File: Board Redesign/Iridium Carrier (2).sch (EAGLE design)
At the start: 154 parts, among them J1 Molex 0541020404, J2 SIM Holder, J3 455-1750-1-ND, J4 CORTEX_DEBUG_SMD, J5 USB_MINI-B_SMT, J6 GND, J7 JST-PA-06-RT, J8 U.FL, Q1 2N7002, Q2 2N7002, Q3 2N7002, U1 LT3959, U2 DAVID-HANDY_ON_NCN4555DEFAULT, U3 TXB0108PWR, U4 ATSAMD21G-A, U5 TXB0108PWR, U6 SX1509, U7 TXB0104RUTR, U8 MCP1826T-3302E/DC, X1 43650-0200, X3 C-GRID-09-70543, Y1 32.768kHz

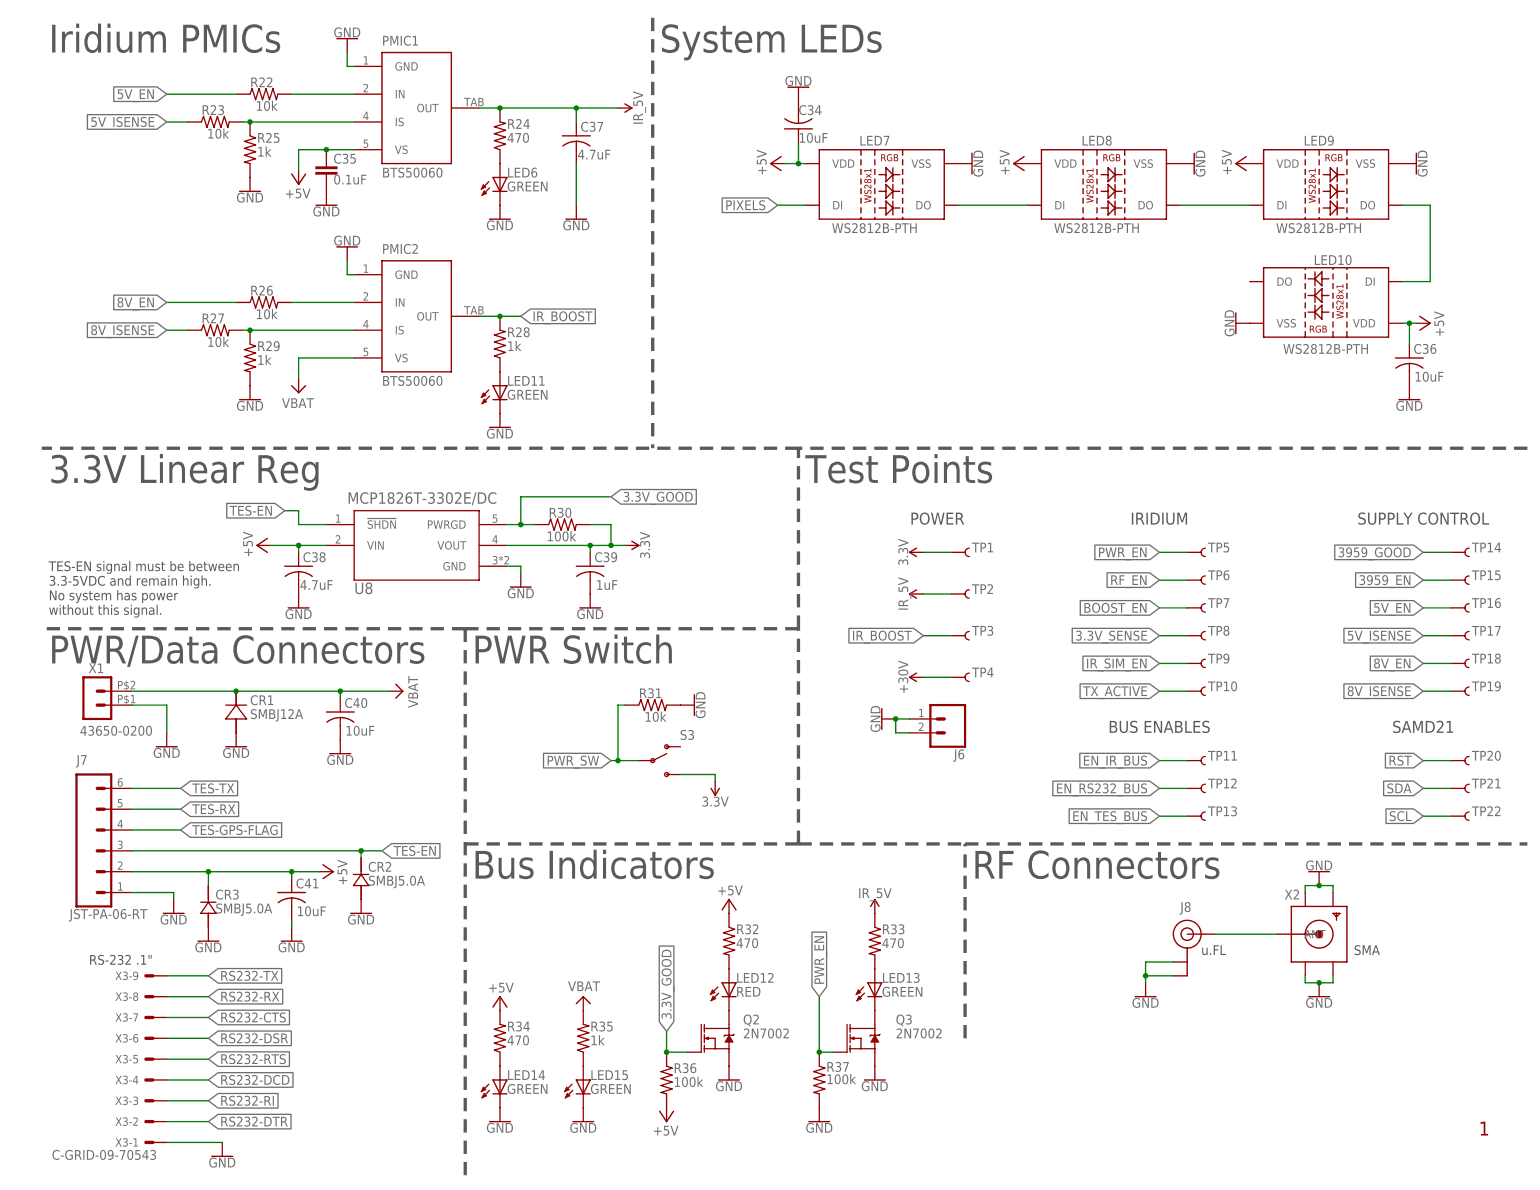
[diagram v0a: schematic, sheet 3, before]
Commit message: Made more progress on board redesign
- Primarily deleted useless (for our purposes) items from the old schematic so we do not have to spend time transferring them over.
- Finished some component transfer
- Renamed some folders
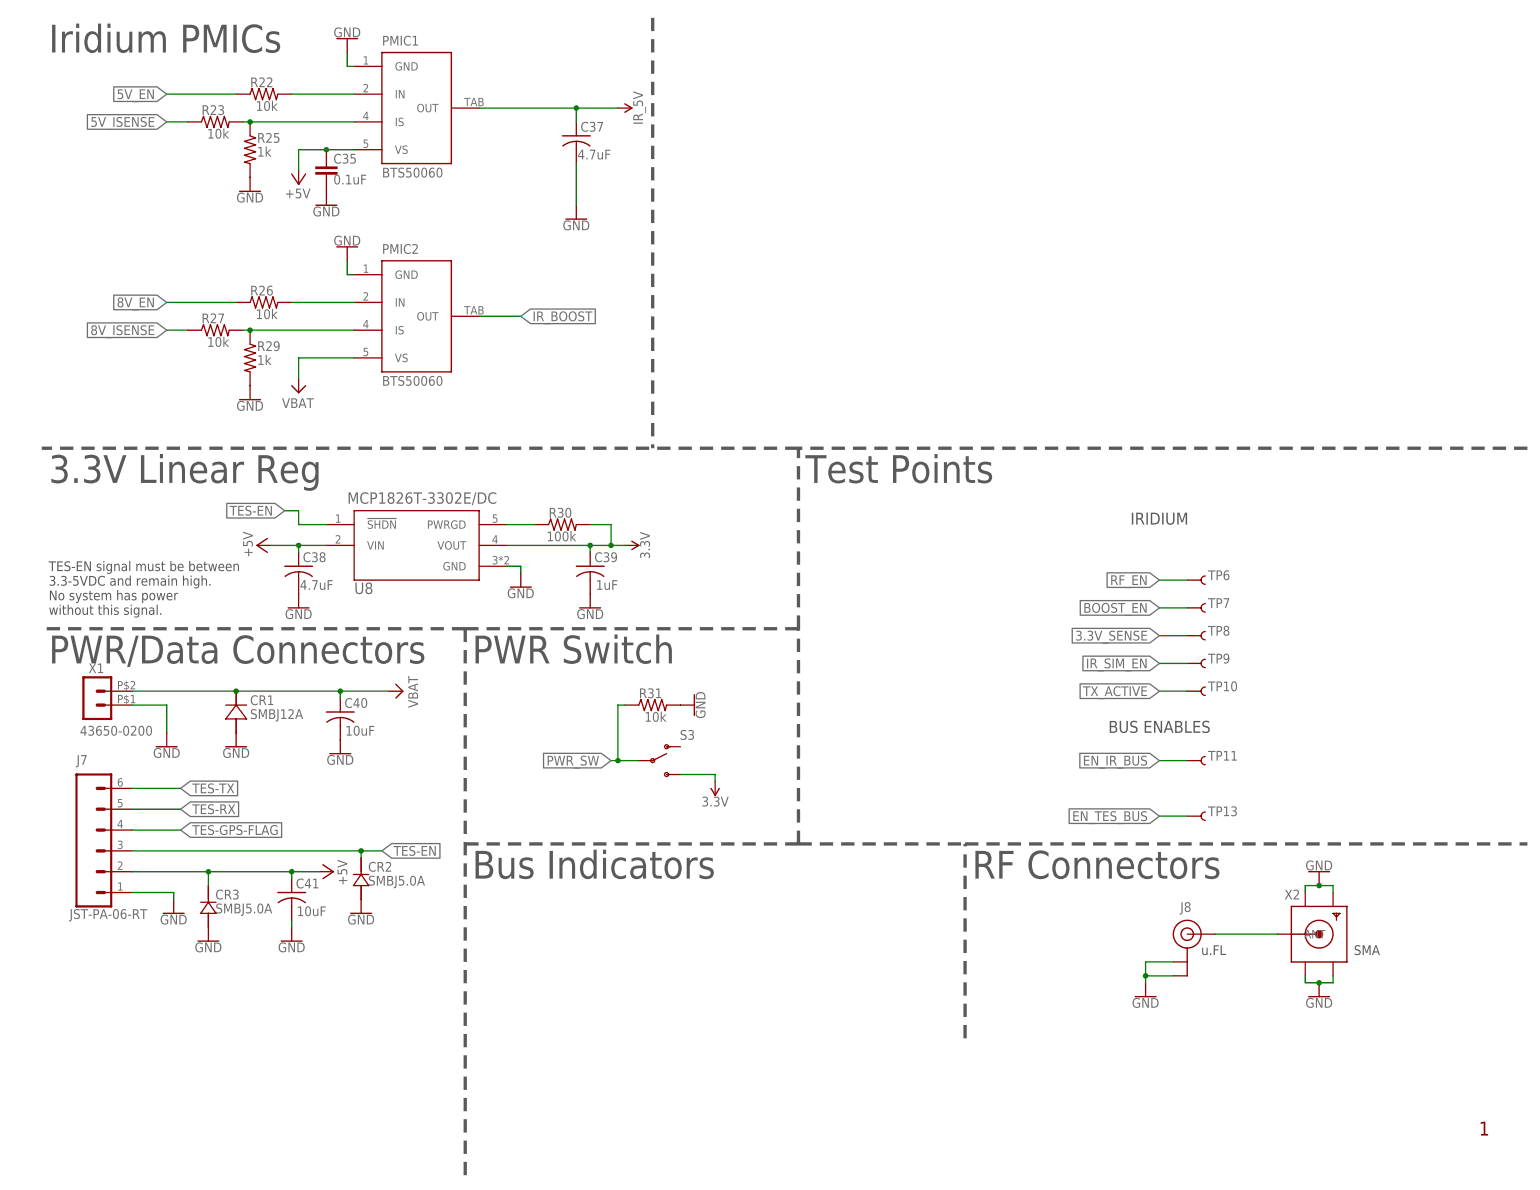
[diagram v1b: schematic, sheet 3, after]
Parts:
- removed C27, C28: 0.1uF, rcl:C-EUC0603
- removed C34, C36: 10uF, adafruit:C-USC1206
- removed J6: GND, SparkFun-Connectors:CONN_02
- removed LED10, LED7, LED8, LED9: WS2812B-PTH, SparkFun-LED:WS2812B-PTH
- removed LED11, LED13, LED14, LED15, LED6: GREEN, adafruit:LEDCHIP-LED0805
- removed LED12: RED, adafruit:LEDCHIP-LED0805
- removed LED2, LED3: BLUE, adafruit:LEDCHIP-LED0805
- removed LED4, LED5: ORANGE, adafruit:LEDCHIP-LED0805
- removed Q2, Q3: 2N7002, SparkFun-DiscreteSemi:MOSFET-NCH-AO3404A
- removed R12: 10k, adafruit:R-US_R0603
- removed R13, R14, R15, R16: 330, adafruit:R-US_R0603
- removed R24, R32, R33, R34: 470, adafruit:R-US_R0603
- removed R28, R35: 1k, adafruit:R-US_R0603
- removed R36, R37: 100k, adafruit:R-US_R0603
- removed TP1, TP12, TP14, TP15, TP16, TP17, TP18, TP19, TP2, TP20, TP21, TP22, TP3, TP4, TP5: TEST-POINT3X4, SparkFun-Connectors:TEST-POINT3X4
- removed U5: TXB0108PWR, TXB0108-PWR:TXB0108PWR
- removed X3: C-GRID-09-70543, con-molex:C-GRID-09-70543
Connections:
- removed net 3.3V_GOOD: Q2.G, R30.1, R36.1, U8.PWRGD
- removed net EN_RS232_BUS: R12.1, TP12.1, U4.PA21(SER5:3+), U5.OE
- removed net I2C_LED: R15.2, U6.I/O[6]
- removed net N$16: LED2.A, R15.1
- removed net N$21: LED4.A, R13.1
- removed net N$22: LED5.A, R14.1
- removed net N$28: LED7.DO, LED8.DI
- removed net N$29: LED8.DO, LED9.DI
- removed net N$32: LED10.DI, LED9.DO
- removed net N$34: LED6.A, R24.1
- removed net N$35: LED14.A, R34.1
- removed net N$36: LED3.A, R16.1
- removed net N$37: LED12.A, R32.2
- removed net N$38: LED12.C, Q2.D
- removed net N$39: LED15.A, R35.1
- removed net N$40: LED11.A, R28.1
- removed net N$41: LED13.A, R33.2
- removed net N$42: LED13.C, Q3.D
- removed net PIXELS: LED7.DI, U4.PA19(SER1:3+)
- removed net RS232-CTS: U5.B6, X3-7.S
- removed net RS232-DCD: U5.B3, X3-4.S
- removed net RS232-DSR: U5.B5, X3-6.S
- removed net RS232-DTR: U5.B1, X3-2.S
- removed net RS232-RI: U5.B2, X3-3.S
- removed net RS232-RTS: U5.B4, X3-5.S
- removed net RS232-RX: U5.B7, X3-8.S
- removed net RS232-TX: U5.B8, X3-9.S
- removed net RX_LED: LED5.C, U4.PB03(AIN11/SER5:1)
- removed net SYS_LED: R16.2, U4.PA17(I2C/SER1:1+)
- removed net TX_LED: LED4.C, U4.PA27
- new net N$12: R30.1, U8.PWRGD
- net !RST: no longer TP20.1
- net +5V: no longer C34.1, C36.1, LED10.VDD, LED7.VDD, LED8.VDD, LED9.VDD, R32.1, R34.2, R36.2
- net 3.3V: no longer C27.2, C28.2, R13.2, R14.2, TP1.1, U5.VCCA, U5.VCCB
- net 3959_EN: no longer TP15.1
- net 3959_GOOD: no longer TP14.1
- net 5V_EN: no longer TP16.1
- net 5V_ISENSE: no longer TP17.1
- net 8V_EN: no longer TP18.1
- net 8V_ISENSE: no longer TP19.1
- net GND: no longer C27.1, C28.1, C34.2, C36.2, J6.1, J6.2, LED10.VSS, LED11.C, LED14.C, LED15.C, LED2.C, LED3.C, LED6.C, LED7.VSS, LED8.VSS, LED9.VSS, Q2.S, Q3.S, R12.2, R37.2, U5.GND, X3-1.S
- net IO-CTS: no longer U5.A6
- net IO-DCD: no longer U5.A3
- net IO-DSR: no longer U5.A5
- net IO-DTR: no longer U5.A1
- net IO-RI: no longer U5.A2
- net IO-RTS: no longer U5.A4
- net IO-RX: no longer U5.A7
- net IO-TX: no longer U5.A8
- net IR_BOOST: no longer R28.2, TP3.1
- net PWR_EN: no longer Q3.G, R37.1, TP5.1
- net SCL: no longer TP22.1
- net SDA: no longer TP21.1
- net VBAT: no longer R35.2
- net VCC: no longer TP4.1
- net V_BATT: no longer R24.2, R33.1, TP2.1
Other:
- note removed: "POWER"
- note removed: "RS-232 .1""
- note removed: "SUPPLY CONTROL"
- note removed: "System LEDs"
